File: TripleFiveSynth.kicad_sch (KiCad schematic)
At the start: 7 parts, among them U1 NE555D

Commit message: ERC and DRC 0 errors
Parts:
- removed C1: 100n, Capacitor_SMD:C_0603_1608Metric, symbol Device:C_Small
- removed C2: 0.01u, Capacitor_SMD:C_0603_1608Metric, symbol Device:C_Small
- removed C3: $val, Capacitor_SMD:C_0603_1608Metric, symbol Device:C_Polarized_Small
- removed R1: 1k, Resistor_SMD:R_0603_1608Metric, symbol Device:R_Small
- removed R2: 9k, Resistor_SMD:R_0603_1608Metric, symbol Device:R_Small
- removed R3: 2k, symbol Device:R_Trim
- removed U1: NE555D, Package_SO:SOIC-8_3.9x4.9mm_P1.27mm, symbol Timer:NE555D
- added J101: Conn_02x26_Odd_Even, Connector_PinHeader_1.27mm:PinHeader_2x26_P1.27mm_Horizontal, symbol Connector_Generic:Conn_02x26_Odd_Even
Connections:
- net GND: now also J101.10 (Pin_10), J101.12 (Pin_12), J101.14 (Pin_14), J101.16 (Pin_16), J101.18 (Pin_18), J101.20 (Pin_20), J101.22 (Pin_22), J101.24 (Pin_24), J101.26 (Pin_26), J101.28 (Pin_28), J101.30 (Pin_30), J101.32 (Pin_32), J101.34 (Pin_34), J101.36 (Pin_36), J101.38 (Pin_38), J101.4 (Pin_4), J101.40 (Pin_40), J101.42 (Pin_42), J101.44 (Pin_44), J101.46 (Pin_46), J101.48 (Pin_48), J101.50 (Pin_50), J101.6 (Pin_6), J101.8 (Pin_8)
- new net +12V: J101.1 (Pin_1), J101.2 (Pin_2), J101.51 (Pin_51), J101.52 (Pin_52)
- new net GATEA: J101.41 (Pin_41)
- new net GATEAS: J101.45 (Pin_45)
- new net GATEB: J101.49 (Pin_49)
- new net GATEC: J101.5 (Pin_5)
- new net GATECS: J101.9 (Pin_9)
- new net GATED: J101.13 (Pin_13)
- new net GATEDS: J101.17 (Pin_17)
- new net GATEE: J101.21 (Pin_21)
- new net GATEF: J101.25 (Pin_25)
- new net GATEFS: J101.29 (Pin_29)
- new net GATEG: J101.33 (Pin_33)
- new net GATEGS: J101.37 (Pin_37)
- new net OUTA: J101.39 (Pin_39)
- new net OUTAS: J101.43 (Pin_43)
- new net OUTB: J101.47 (Pin_47)
- new net OUTC: J101.3 (Pin_3)
- new net OUTCS: J101.7 (Pin_7)
- new net OUTD: J101.11 (Pin_11)
- new net OUTDS: J101.15 (Pin_15)
- new net OUTE: J101.19 (Pin_19)
- new net OUTEG: J101.31 (Pin_31)
- new net OUTF: J101.23 (Pin_23)
- new net OUTFS: J101.27 (Pin_27)
- new net OUTGS: J101.35 (Pin_35)
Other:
- added sheet Voice (Voice.kicad_sch)
- added sheet Voice1 (Voice.kicad_sch)
- added sheet Voice10 (Voice.kicad_sch)
- added sheet Voice11 (Voice.kicad_sch)
- added sheet Voice2 (Voice.kicad_sch)
- added sheet Voice3 (Voice.kicad_sch)
- added sheet Voice4 (Voice.kicad_sch)
- added sheet Voice5 (Voice.kicad_sch)
- added sheet Voice6 (Voice.kicad_sch)
- added sheet Voice7 (Voice.kicad_sch)
- added sheet Voice8 (Voice.kicad_sch)
- added sheet Voice9 (Voice.kicad_sch)
- note added: "A"
- note added: "A#"
- note added: "B"
- note added: "C"
- note added: "C#"
- note added: "D"
- note added: "D#"
- note added: "E"
- note added: "F"
- note added: "F#"
- note added: "G"
- note added: "G#"
- note removed: "% from tune_triple_fives.txt"
- note removed: "value from tune_triple_fives.txt"

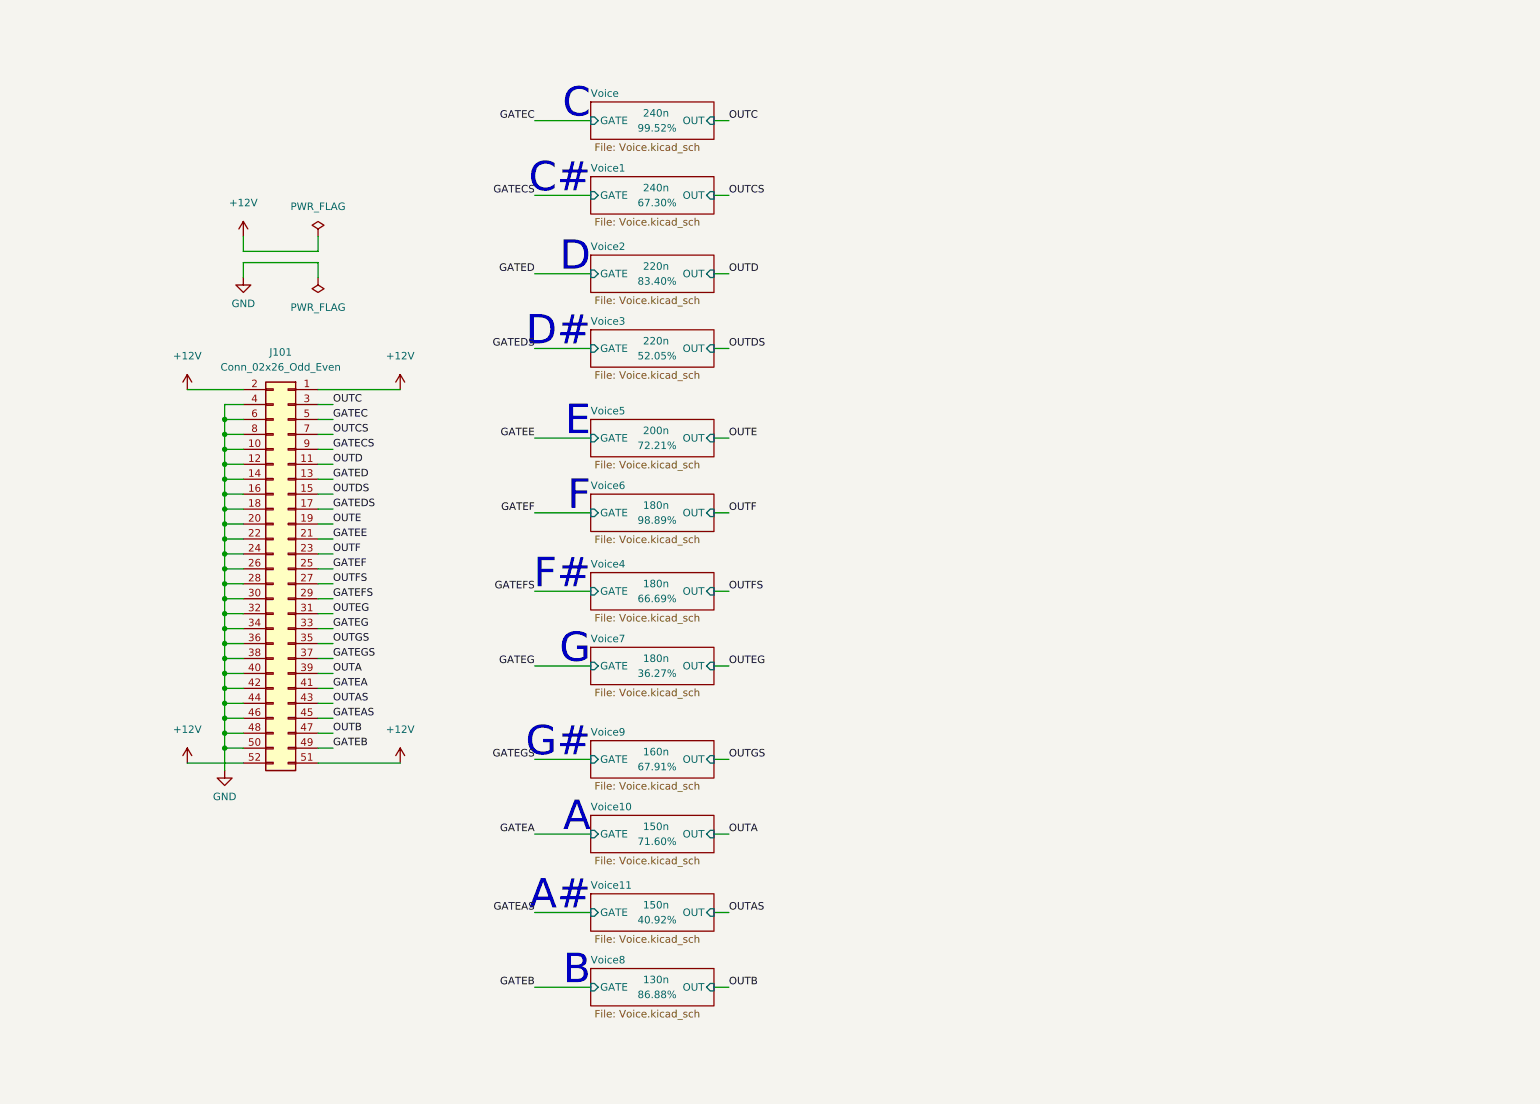
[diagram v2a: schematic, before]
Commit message: update with 5V and on-board sum
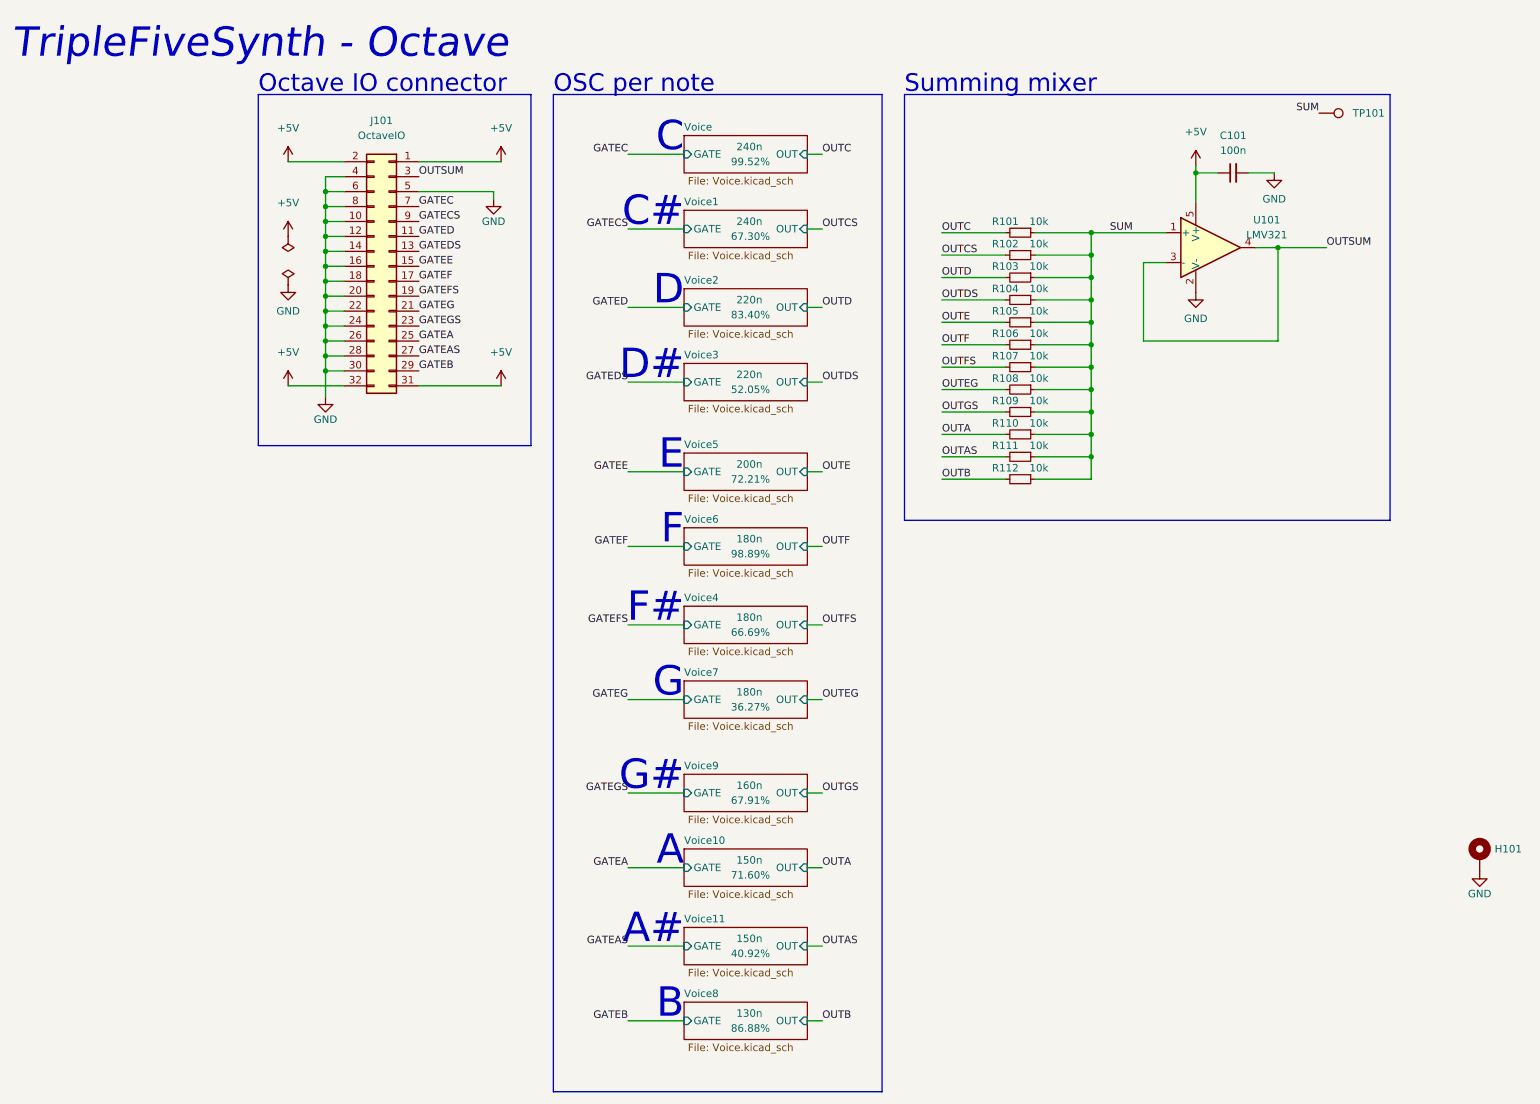
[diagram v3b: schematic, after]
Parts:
- removed J101: Conn_02x26_Odd_Even, Connector_PinHeader_1.27mm:PinHeader_2x26_P1.27mm_Horizontal, symbol Connector_Generic:Conn_02x26_Odd_Even
- added C101: 100n, Capacitor_SMD:C_0402_1005Metric, symbol Device:C_Small
- added H101: MountingHole_Pad, MountingHole:MountingHole_2.2mm_M2_ISO7380_Pad, symbol Mechanical:MountingHole_Pad
- added J101: OctaveIO, Connector_PinHeader_1.27mm:PinHeader_2x16_P1.27mm_Horizontal, symbol Connector_Generic:Conn_02x16_Odd_Even
- added R101, R102, R103, R104, R105, R106, R107, R108, R109, R110, R111, R112: 10k, Resistor_SMD:R_0603_1608Metric, symbol Device:R_Small
- added TP101: SUM, TestPoint:TestPoint_Pad_D1.0mm, symbol Connector:TestPoint
- added U101: LMV321, Package_TO_SOT_SMD:SOT-23-5, symbol Amplifier_Operational:LMV321
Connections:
- net GATEA: now also J101.25 (Pin_25)
- net GATEAS: now also J101.27 (Pin_27)
- net GATEB: now also J101.29 (Pin_29)
- net GATEC: now also J101.7 (Pin_7)
- net GATECS: now also J101.9 (Pin_9)
- net GATED: now also J101.11 (Pin_11)
- net GATEDS: now also J101.13 (Pin_13)
- net GATEE: now also J101.15 (Pin_15)
- net GATEF: now also J101.17 (Pin_17)
- net GATEFS: now also J101.19 (Pin_19)
- net GATEG: now also J101.21 (Pin_21)
- net GATEGS: now also J101.23 (Pin_23)
- net GND: now also C101.2, H101.1, J101.10 (Pin_10), J101.12 (Pin_12), J101.14 (Pin_14), J101.16 (Pin_16), J101.18 (Pin_18), J101.20 (Pin_20), J101.22 (Pin_22), J101.24 (Pin_24), J101.26 (Pin_26), J101.28 (Pin_28), J101.30 (Pin_30), J101.4 (Pin_4), J101.5 (Pin_5), J101.6 (Pin_6), J101.8 (Pin_8), U101.2 (V-)
- net OUTA: now also R110.2
- net OUTAS: now also R111.2
- net OUTB: now also R112.2
- net OUTC: now also R101.2
- net OUTCS: now also R102.2
- net OUTD: now also R103.2
- net OUTDS: now also R104.2
- net OUTE: now also R105.2
- net OUTEG: now also R108.2
- net OUTF: now also R106.2
- net OUTFS: now also R107.2
- net OUTGS: now also R109.2
- new net +5V: C101.1, J101.1 (Pin_1), J101.2 (Pin_2), J101.31 (Pin_31), J101.32 (Pin_32), U101.5 (V+)
- new net OUTSUM: J101.3 (Pin_3), U101.3 (-), U101.4
- new net SUM: R101.1, R102.1, R103.1, R104.1, R105.1, R106.1, R107.1, R108.1, R109.1, R110.1, R111.1, R112.1, TP101.1, U101.1 (+)
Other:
- note added: "OSC per note"
- note added: "Octave IO connector"
- note added: "Summing mixer"
- note added: "TripleFiveSynth - Octave"
- company: (none) -> Alexander Brevig
- title: (none) -> TripleFiveSynth - Octave
